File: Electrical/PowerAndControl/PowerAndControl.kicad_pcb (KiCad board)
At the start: 2 copper layers, 65 x 30 mm, 26 parts, among them J1 Conn_02x03_Counter_Clockwise, SW2 SW_SPDT_312, U1 STC4054GR, U2 TPS22919QDCKRQ1, U3 TPS3840PL30DBVR

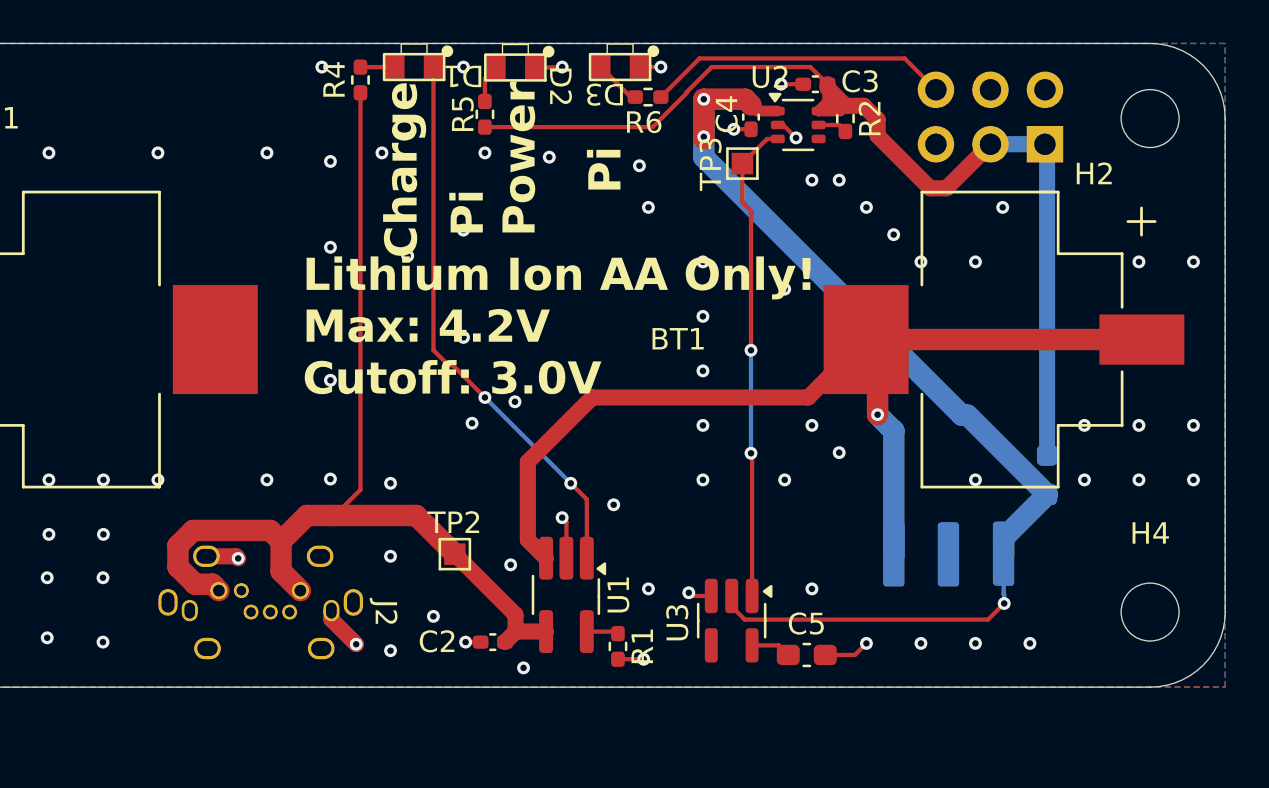
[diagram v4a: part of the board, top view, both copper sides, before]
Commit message: Rerouted Switch, Added Thermostat
Switch is now on the same side as the USB port. Should help
reduce z axis stackup.
Added thermostat, will shutoff if high temp
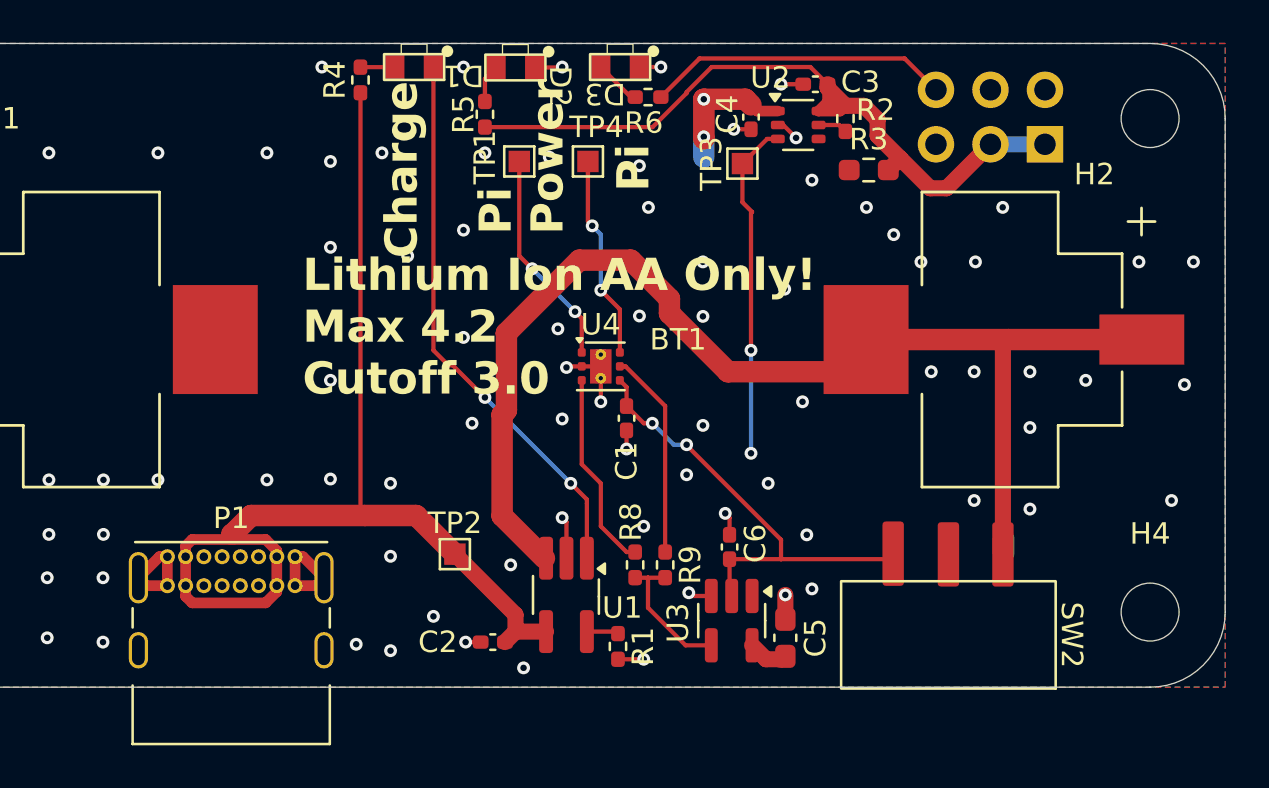
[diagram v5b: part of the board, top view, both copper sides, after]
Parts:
- removed J2: ~, Library:10176783-00011LF
- added C1: 0.1u, Capacitor_SMD:C_0402_1005Metric_Pad0.74x0.62mm_HandSolder, F.Cu at (133.6, 114.0)
- added C6: 0.1u, Capacitor_SMD:C_0402_1005Metric_Pad0.74x0.62mm_HandSolder, F.Cu at (138.4, 120.0)
- added P1: USB_C_Plug_USB2.0, Connector_USB:USB_C_Receptacle_GCT_USB4085, F.Cu at (112.2, 120.4)
- added R8: 0, Resistor_SMD:R_0402_1005Metric_Pad0.72x0.64mm_HandSolder, F.Cu at (134.0, 120.8)
- added R9: 0, Resistor_SMD:R_0402_1005Metric_Pad0.72x0.64mm_HandSolder, F.Cu at (135.4, 120.8)
- added TP1: TestPoint, TestPoint:TestPoint_Pad_1.0x1.0mm, F.Cu at (128.6, 102.0)
- added TP4: TestPoint, TestPoint:TestPoint_Pad_1.0x1.0mm, F.Cu at (131.8, 102.0)
- added U4: LM26LVCISD-050, Package_SON:WSON-6-1EP_2x2mm_P0.65mm_EP1x1.6mm_ThermalVias, F.Cu at (132.4, 111.5)
- R3, SW2: moved to F.Cu
- moved R3 16.5 mm to (144.9, 102.4), turned to 0 degrees
- moved C5 1.28 mm to (141.0, 124.2), turned to 90 degrees
- turned SW2 to 180 degrees
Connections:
- U3 pad 4: unconnected-(U3-MR_N-Pad4) -> /TEMP
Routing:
- net /VBAT: track 50.4 -> 31.0 mm, vias 3 -> 4
- net /VBAT_OUT: track 49.4 -> 35.8 mm
- net Net-(U4-TRIP_TEST): track 0.00 -> 10.1 mm, vias 0 -> 2
- net /VBAT_PRESWITCH: track 46.4 -> 56.5 mm, vias 1 -> 0
- net Net-(U4-OVERTEMP): track 0.00 -> 9.68 mm
- net Net-(U4-VTEMP): track 0.00 -> 9.52 mm, vias 0 -> 2
- net GND: track 15.9 -> 25.2 mm, vias 78 -> 79
- net Net-(U4-~OVERTEMP): track 0.00 -> 9.27 mm
- net /MONITOR: track 22.5 -> 15.9 mm
- net /TEMP: track 0.00 -> 6.48 mm
- net VBUS: track 47.8 -> 51.6 mm
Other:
- board text added: "*TECHNICALLY violating the clearence of the battery package. However. WSON is 0.8mm tall. The bottom of the battery clip is at 0.85mm."
- board text added: "Lithium Ion AA Only! Max 4.2 Cutoff 3.0"
- board text removed: "Lithium Ion AA Only! Max: 4.2V Cutoff: 3.0V"

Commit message: Fixed up / Repositioned Model
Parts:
- added R7: 100k, Resistor_SMD:R_0402_1005Metric_Pad0.72x0.64mm_HandSolder, F.Cu at (136.8, 119.4)
- moved SW2 0.90 mm to (148.6, 121.2)
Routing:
- net /VBAT: track 31.0 -> 85.8 mm, vias 4 -> 6
- net /TEMP: track 6.48 -> 8.46 mm
- net /VBAT_PRESWITCH: track 56.5 -> 57.4 mm
- net GND: vias 79 -> 76

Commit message: Fixed Minor Issue. Getting Fabbed
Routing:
- net GND: track 25.2 -> 33.1 mm, vias 76 -> 87
- net /MONITOR: track 15.9 -> 23.1 mm
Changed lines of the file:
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@@
 		(at 129.318935 97.62 180)
 		(property "Reference" "D2"
-			(at -1.181065 -0.88 270)
+			(at -1.681065 -0.38 270)
 			(unlocked yes)
 			(layer "F.SilkS")
@@
 	)
 	(segment
+		(start 112.2 120.42)
+		(end 112.2 118.6)
+		(width 0.5)
+		(layer "F.Cu")
+		(net 2)
+	)
+	(segment
 		(start 119.13 121.77)
 		(end 119.5 121.4)
@@
 	)
 	(segment
+		(start 118.15 123.15)
+		(end 118.2 123.2)
+		(width 0.5)
+		(layer "F.Cu")
+		(net 2)
+	)
+	(segment
 		(start 130.58 97.62)
 		(end 130.6 97.6)
@@
 	)
 	(segment
+		(start 118.15 120.42)
+		(end 118.97 119.6)
+		(width 0.5)
+		(layer "F.Cu")
+		(net 2)
+	)
+	(segment
 		(start 134.2 97.6)
 		(end 135.2 97.6)
@@
 	)
 	(segment
+		(start 118.97 119.6)
+		(end 121 119.6)
+		(width 0.5)
+		(layer "F.Cu")
+		(net 2)
+	)
+	(segment
+		(start 112.2 121.77)
+		(end 112.2 123.2)
+		(width 0.5)
+		(layer "F.Cu")
+		(net 2)
+	)
+	(segment
 		(start 133.2 125.2)
 		(end 134.4 125.2)
@@
 	)
 	(segment
+		(start 118.15 121.77)
+		(end 118.15 123.15)
+		(width 0.5)
+		(layer "F.Cu")
+		(net 2)
+	)
+	(segment
 		(start 111.22 121.77)
 		(end 110.85 121.4)
@@
 	)
 	(via
+		(at 136.6 100)
+		(size 0.6)
+		(drill 0.3)
+		(layers "F.Cu" "B.Cu")
+		(free yes)
+		(net 2)
+	)
+	(via
 		(at 128.8 125.6)
 		(size 0.6)
@@
 	)
 	(via
+		(at 148 108.8)
+		(size 0.6)
+		(drill 0.3)
+		(layers "F.Cu" "B.Cu")
+		(free yes)
+		(net 2)
+	)
+	(via
 		(at 106.6 124.2)
 		(size 0.6)
@@
 	)
 	(via
+		(at 121 119.6)
+		(size 0.6)
+		(drill 0.3)
+		(layers "F.Cu" "B.Cu")
+		(net 2)
+	)
+	(via
 		(at 109.22 119.38)
 		(size 0.6)
@@
 	)
 	(via
+		(at 137 108.6)
+		(size 0.6)
+		(drill 0.3)
+		(layers "F.Cu" "B.Cu")
+		(free yes)
+		(net 2)
+	)
+	(via
 		(at 119.8 102)
 		(size 0.6)
@@
 	)
 	(via
+		(at 138.4 110)
+		(size 0.6)
+		(drill 0.3)
+		(layers "F.Cu" "B.Cu")
+		(free yes)
+		(net 2)
+	)
+	(via
 		(at 111.76 116.84)
 		(size 0.6)
@@
 	)
 	(via
-		(at 149.8 117.8)
+		(at 112.2 118.6)
 		(size 0.6)
 		(drill 0.3)
 		(layers "F.Cu" "B.Cu")
-		(free yes)
 		(net 2)
 	)
 	(via
-		(at 132.4 113.2)
+		(at 149.8 117.8)
 		(size 0.6)
 		(drill 0.3)
@@
 	)
 	(via
-		(at 106.68 119.38)
+		(at 132.4 113.2)
 		(size 0.6)
 		(drill 0.3)
@@
 	)
 	(via
-		(at 151.13 104.14)
+		(at 106.68 119.38)
 		(size 0.6)
 		(drill 0.3)
@@
 	)
 	(via
-		(at 116.84 101.6)
+		(at 151.13 104.14)
 		(size 0.6)
 		(drill 0.3)
@@
 	)
 	(via
-		(at 140.2 117)
+		(at 116.84 101.6)
 		(size 0.6)
 		(drill 0.3)
@@
 	)
 	(via
-		(at 155 112.2)
+		(at 140.2 117)
 		(size 0.6)
 		(drill 0.3)
@@
 	)
 	(via
+		(at 154.4 122.8)
+		(size 0.6)
+		(drill 0.3)
+		(layers "F.Cu" "B.Cu")
+		(free yes)
+		(net 2)
+	)
+	(via
 		(at 134.62 104.14)
 		(size 0.6)
@@
 	)
 	(via
+		(at 144.4 119.4)
+		(size 0.6)
+		(drill 0.3)
+		(layers "F.Cu" "B.Cu")
+		(free yes)
+		(net 2)
+	)
+	(via
+		(at 156 116.8)
+		(size 0.6)
+		(drill 0.3)
+		(layers "F.Cu" "B.Cu")
+		(free yes)
+		(net 2)
+	)
+	(via
 		(at 134.4 125.2)
 		(size 0.6)
@@
 	)
 	(via
-		(at 142.24 121.92)
+		(at 144.4 121.6)
 		(size 0.6)
 		(drill 0.3)
@@
 	)
 	(via
-		(at 137.16 109.22)
+		(at 136.5 122.1)
 		(size 0.6)
 		(drill 0.3)
 		(layers "F.Cu" "B.Cu")
-		(free yes)
 		(net 2)
 	)
 	(via
-		(at 136.5 122.1)
+		(at 122.6 124.8)
 		(size 0.6)
 		(drill 0.3)
 		(layers "F.Cu" "B.Cu")
+		(free yes)
 		(net 2)
 	)
 	(via
-		(at 122.6 124.8)
+		(at 137.16 114.3)
 		(size 0.6)
 		(drill 0.3)
@@
 	)
 	(via
-		(at 137.16 114.3)
+		(at 126.4 114.2)
 		(size 0.6)
 		(drill 0.3)
@@
 	)
 	(via
-		(at 126.4 114.2)
+		(at 118.2 123.2)
 		(size 0.6)
 		(drill 0.3)
 		(layers "F.Cu" "B.Cu")
-		(free yes)
 		(net 2)
 	)
@@
 	)
 	(via
-		(at 152.4 114.4)
+		(at 152.4 115.2)
 		(size 0.6)
 		(drill 0.3)
@@
 	)
 	(via
+		(at 141.8 110.4)
+		(size 0.6)
+		(drill 0.3)
+		(layers "F.Cu" "B.Cu")
+		(free yes)
+		(net 2)
+	)
+	(via
 		(at 134.4 119)
 		(size 0.6)
@@
 	)
 	(via
+		(at 112.2 123.2)
+		(size 0.6)
+		(drill 0.3)
+		(layers "F.Cu" "B.Cu")
+		(net 2)
+	)
+	(via
 		(at 122.6 117)
 		(size 0.6)
@@
 	)
 	(via
-		(at 137.16 106.68)
+		(at 128.2 99.4)
 		(size 0.6)
 		(drill 0.3)
@@
 	)
 	(via
+		(at 132.8 99.4)
+		(size 0.6)
+		(drill 0.3)
+		(layers "F.Cu" "B.Cu")
+		(free yes)
+		(net 2)
+	)
+	(via
 		(at 106.68 101.6)
 		(size 0.6)
@@
 	)
 	(segment
+		(start 115.231 119.369)
+		(end 116.1 118.5)
+		(width 1)
+		(layer "F.Cu")
+		(net 3)
+	)
+	(segment
 		(start 117.3 122.052786)
 		(end 117.3 121.77)
@@
 	)
 	(segment
-		(start 116.1 118.5)
-		(end 115.231 119.369)
-		(width 1)
-		(layer "F.Cu")
-		(net 3)
-	)
-	(segment
 		(start 128.425 123.125)
 		(end 125.6 120.3)
@@
 	)
 	(segment
-		(start 139.45 115.65)
-		(end 139.4 115.6)
+		(start 140.2 121.2)
+		(end 140.2 121.5)
 		(width 0.2)
 		(layer "F.Cu")
@@
 	)
 	(segment
+		(start 140.2 121.5)
+		(end 139.45 122.25)
+		(width 0.2)
+		(layer "F.Cu")
+		(net 9)
+	)
+	(segment
 		(start 139.4 104.4)
 		(end 139.45 104.35)
@@
 	)
 	(via
-		(at 139.4 115.6)
+		(at 140.2 121.2)
 		(size 0.6)
 		(drill 0.3)
@@
 		(width 0.2)
 		(layer "B.Cu")
+		(net 9)
+	)
+	(segment
+		(start 139.4 115.6)
+		(end 139.4 120.4)
+		(width 0.2)
+		(layer "B.Cu")
+		(net 9)
+	)
+	(segment
+		(start 139.4 120.4)
+		(end 140.2 121.2)
+		(width 0.2)
+		(layer "B.Cu")
